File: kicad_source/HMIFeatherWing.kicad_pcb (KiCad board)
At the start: 2 copper layers, 67 x 30 mm, 29 parts, among them CN1 ADAFRUIT_FEATHER, Q1 2N7002, SW1 ALPS_SKRH, SW2 SW_PUSH

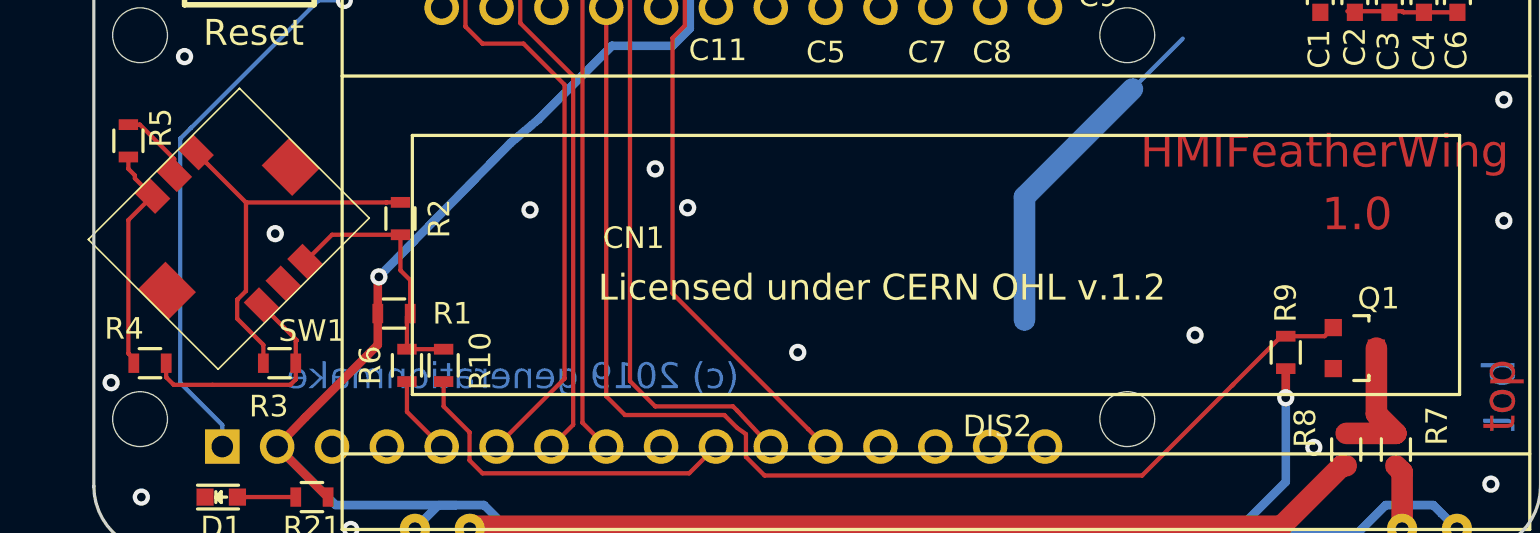
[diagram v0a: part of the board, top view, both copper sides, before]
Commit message: started development for 1.1, made pads for ALPS SKRH a little bit longer
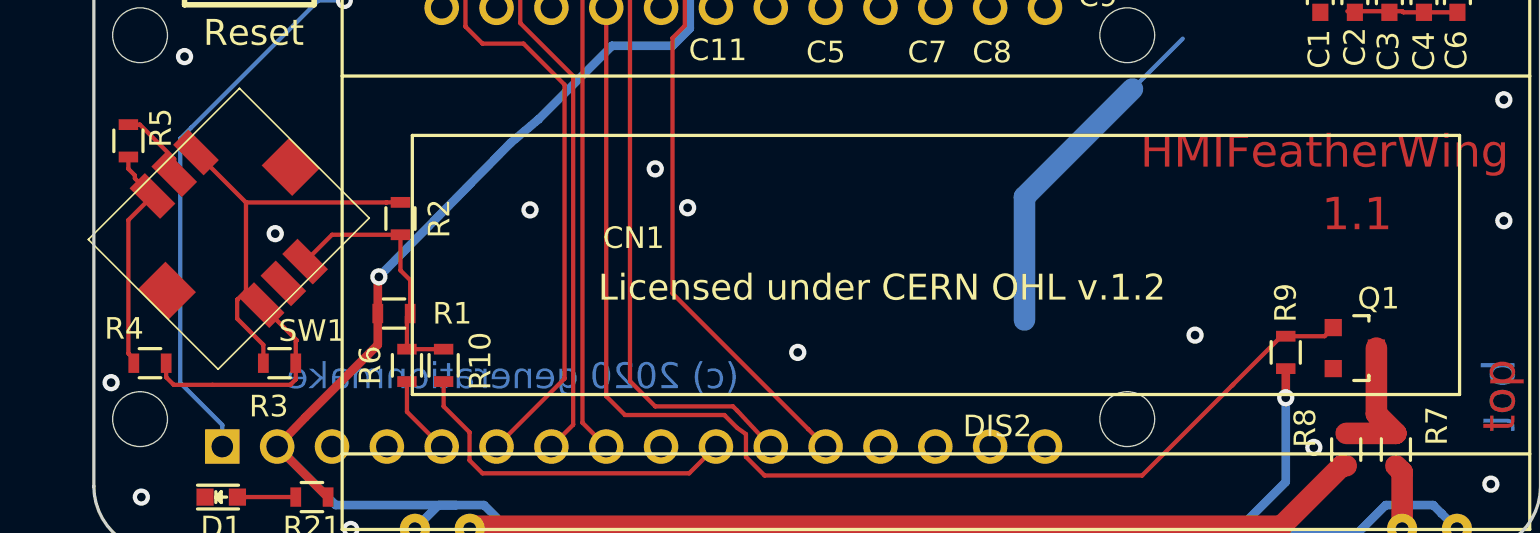
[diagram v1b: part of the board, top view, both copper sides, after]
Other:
- board text added: "(c) 2020 generationmake"
- board text added: "1.1"
- board text removed: "(c) 2019 generationmake"
- board text removed: "1.0"
